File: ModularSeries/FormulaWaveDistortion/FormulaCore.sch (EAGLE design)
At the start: 68 parts, among them Q1 2N3906, Q2 2N3904, Q3 2N3906, Q4 2N3904

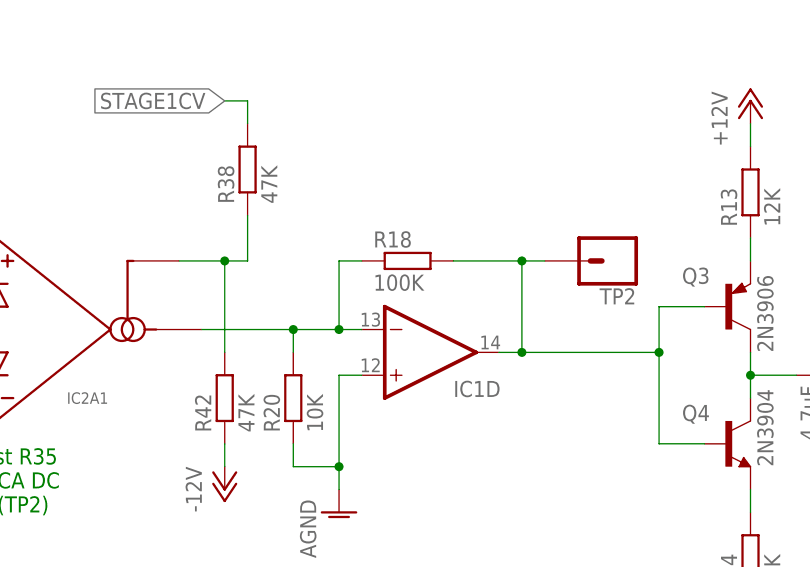
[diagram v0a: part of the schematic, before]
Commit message: Formula resistor error corrected in affected files
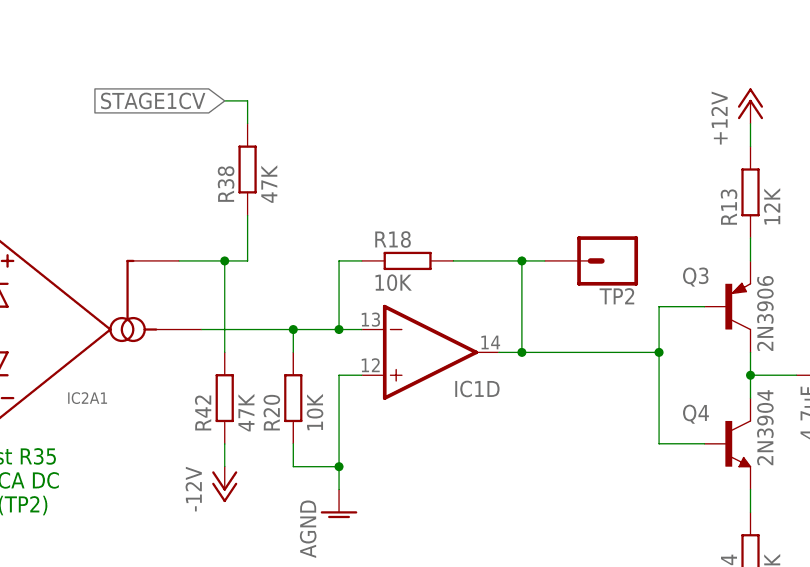
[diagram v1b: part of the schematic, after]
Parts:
- R18: value 100K -> 10K
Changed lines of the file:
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@@
 <part name="IC2" library="ElectricNoodleBox" deviceset="LM13700" device="DIL" package3d_urn="urn:adsk.eagle:package:922/2"/>
 <part name="R17" library="rcl" library_urn="urn:adsk.eagle:library:334" deviceset="R-EU_" device="0207/7" package3d_urn="urn:adsk.eagle:package:23493/2" value="10K"/>
-<part name="R18" library="rcl" library_urn="urn:adsk.eagle:library:334" deviceset="R-EU_" device="0207/7" package3d_urn="urn:adsk.eagle:package:23493/2" value="100K"/>
+<part name="R18" library="rcl" library_urn="urn:adsk.eagle:library:334" deviceset="R-EU_" device="0207/7" package3d_urn="urn:adsk.eagle:package:23493/2" value="10K"/>
 <part name="AGND4" library="supply1" library_urn="urn:adsk.eagle:library:371" deviceset="AGND" device=""/>
 <part name="AGND5" library="supply1" library_urn="urn:adsk.eagle:library:371" deviceset="AGND" device=""/>
